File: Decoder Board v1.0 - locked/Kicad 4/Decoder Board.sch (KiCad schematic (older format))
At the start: 215 parts, among them P201 CONN_01X02, P202 JTAG, P203 CONN_02X20, U201 EPM240, U202 AP1117D33

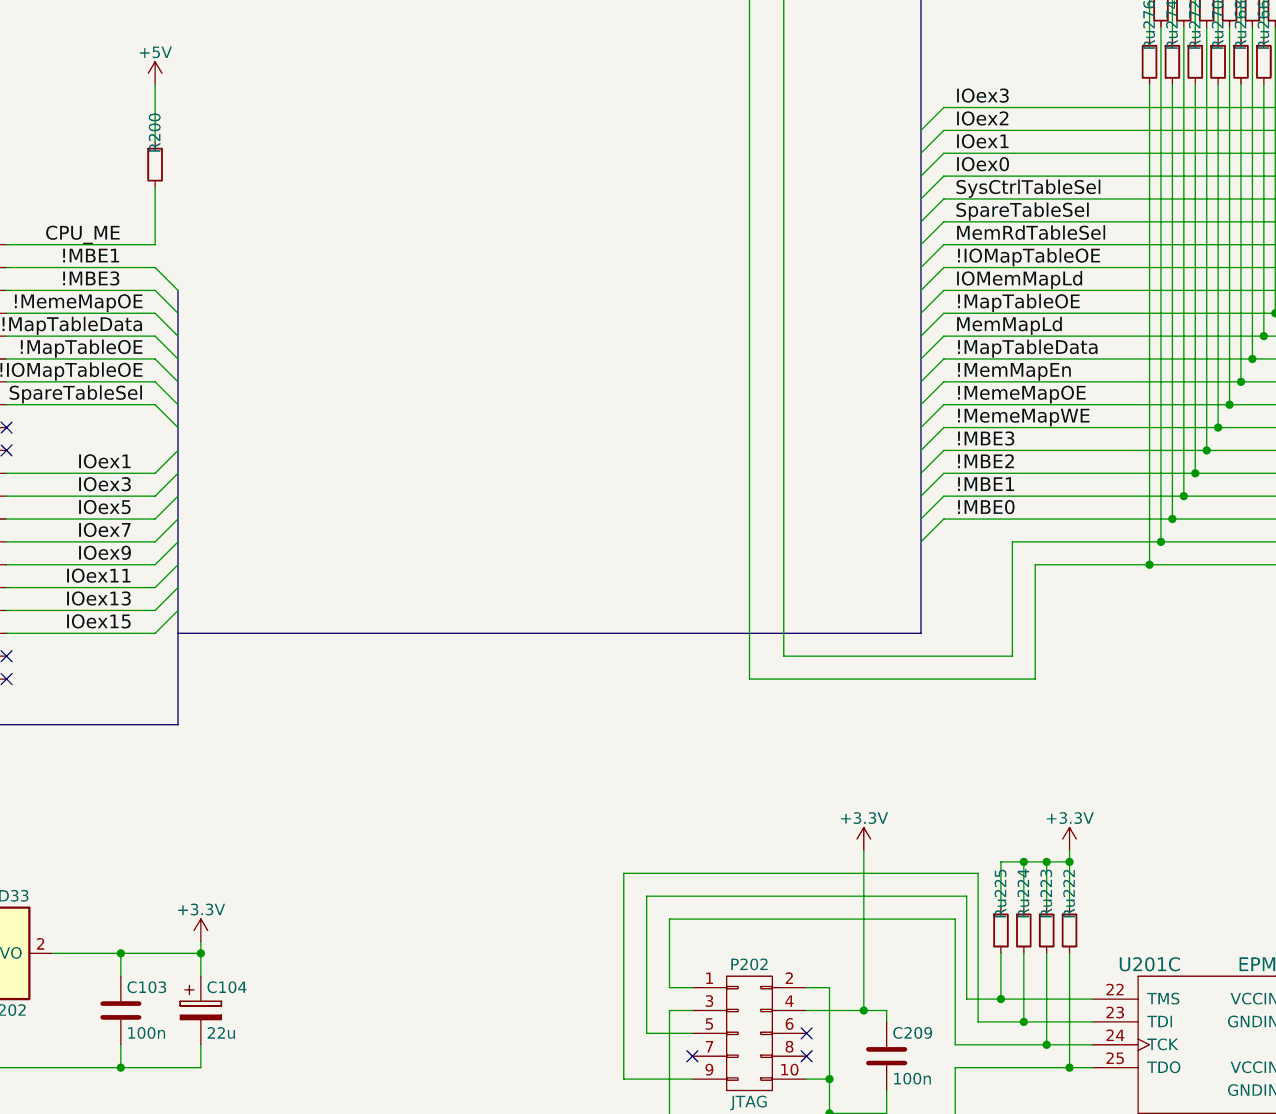
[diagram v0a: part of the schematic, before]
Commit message: memmgr u101 latch timing issue
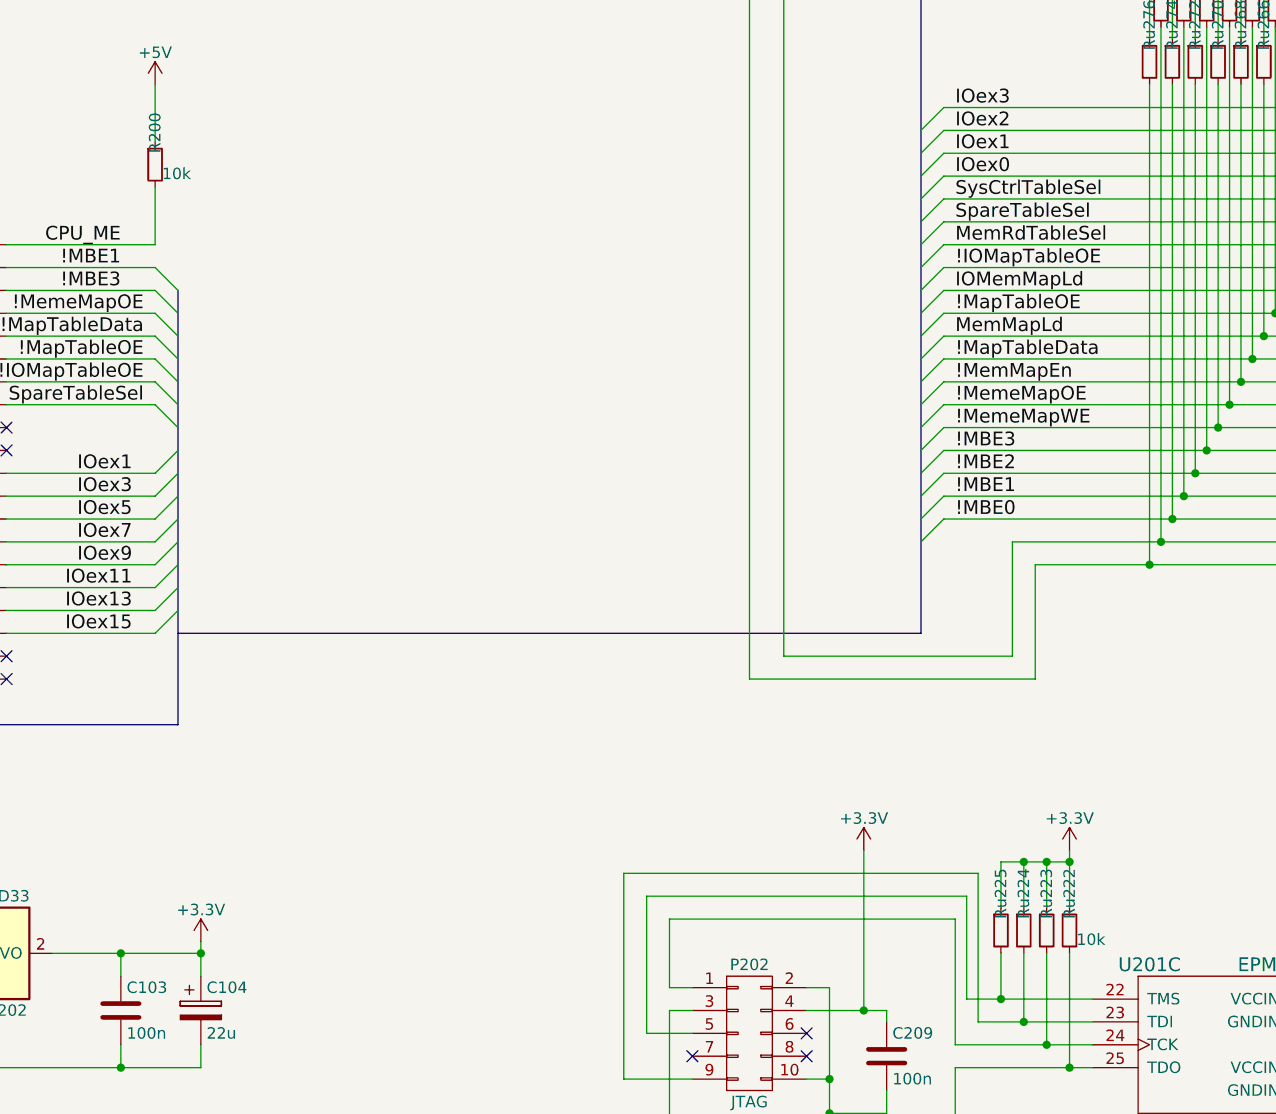
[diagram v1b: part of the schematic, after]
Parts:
- R200, Ru222: value (none) -> 10k
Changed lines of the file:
@@
 P 4200 6250
 F 0 "R200" V 4200 6300 50  0000 L CNN
-F 1 " " H 4230 6210 50  0000 L CNN
+F 1 "10k " H 4230 6210 50  0000 L CNN
 F 2 "Resistors_SMD:R_0603_HandSoldering" H 4200 6250 50  0001 C CNN
 F 3 "" H 4200 6250 50  0000 C CNN
@@
 P 8200 9600
 F 0 "Ru222" V 8200 9650 50  0000 L CNN
-F 1 " " H 8230 9560 50  0000 L CNN
+F 1 "10k " H 8230 9560 50  0000 L CNN
 F 2 "Resistors_SMD:R_0603_HandSoldering" H 8200 9600 50  0001 C CNN
 F 3 "" H 8200 9600 50  0000 C CNN
